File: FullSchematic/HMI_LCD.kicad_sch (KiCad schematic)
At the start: 31 parts, among them J10 LCD_Conn, J9 2x6 Pin Header, Q3 NPN, U10 SN74LVC2T45DCURE4, U11 SN74LVC2T45DCURE4, U12 SN74LVC2T45DCURE4, U13 SN74LVC2T45DCURE4, U14 SN74LV595ARGYR, U9 L79L05ABD13TR

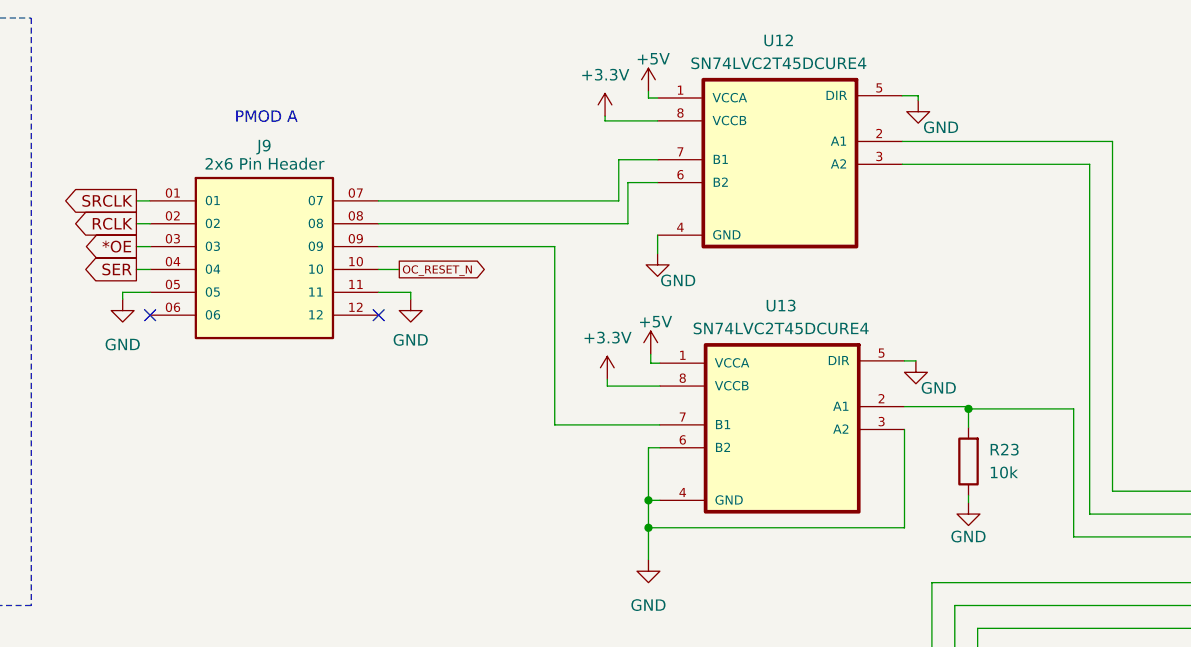
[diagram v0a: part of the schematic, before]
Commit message: Schematic/Footprint Update
Corrected Footprint / Schematic for PCB Design and Changed 10k Resistors to 0603 size.
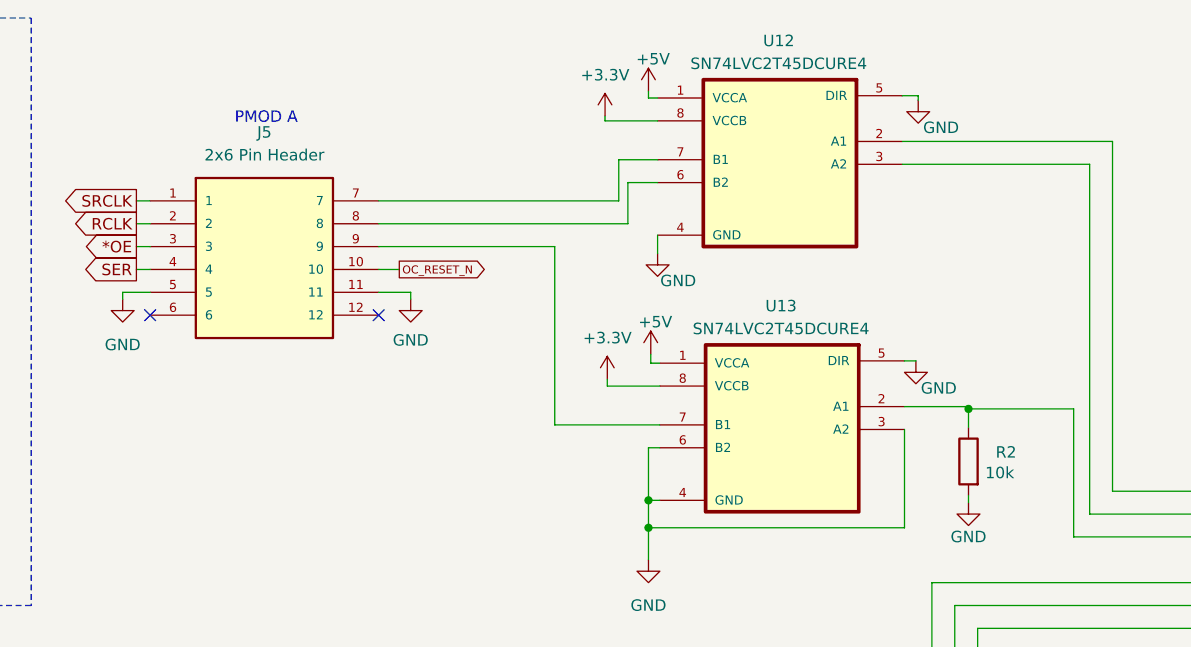
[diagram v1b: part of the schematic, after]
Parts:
- removed J9: 2x6 Pin Header, Connector_PinHeader_2.54mm:PinHeader_2x06_P2.54mm_Vertical, symbol SFMC-106-L2-L-D:SFMC-106-L2-L-D
- removed R23: 10k, Resistor_SMD:R_1206_3216Metric, symbol Device:R
- added J5: 2x6 Pin Header, Connector_PinHeader_2.54mm:PinHeader_2x06_P2.54mm_Vertical, symbol SFMC-106-L2-L-D:SFMC-106-L2-L-D
- added R2: 10k, Resistor_SMD:R_0201_0603Metric, symbol Device:R
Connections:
- net *OE: now also J5.3
- net GND: now also J5.11, J5.5, R2.2
- net OC_RESET_N: now also J5.10
- net RCLK: now also J5.2
- net SER: now also J5.4
- net SRCLK: now also J5.1
- net at J10.6 (E), U13.2 (A1): now also R2.1
- net at U13.7 (B1): now also J5.9
- net at U12.6 (B2): now also J5.8
- net at U12.7 (B1): now also J5.7

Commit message: Semi-complete board
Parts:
- J5: footprint Connector_PinHeader_2.54mm:PinHeader_2x06_P2.54mm_Vertical -> CustomFootprints:PMOD
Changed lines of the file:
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@@
       (effects (font (size 1.27 1.27)))
     )
-    (property "Footprint" "Connector_PinHeader_2.54mm:PinHeader_2x06_P2.54mm_Vertical" (at 118.0592 51.816 0)
+    (property "Footprint" "CustomFootprints:PMOD" (at 118.0592 51.816 0)
       (effects (font (size 1.27 1.27)) (justify bottom) hide)
     )

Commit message: PCB V.1
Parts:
- removed C3 (x4): .01u, Capacitor_SMD:C_0805_2012Metric, symbol Device:C
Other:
- moved on the sheet: C3

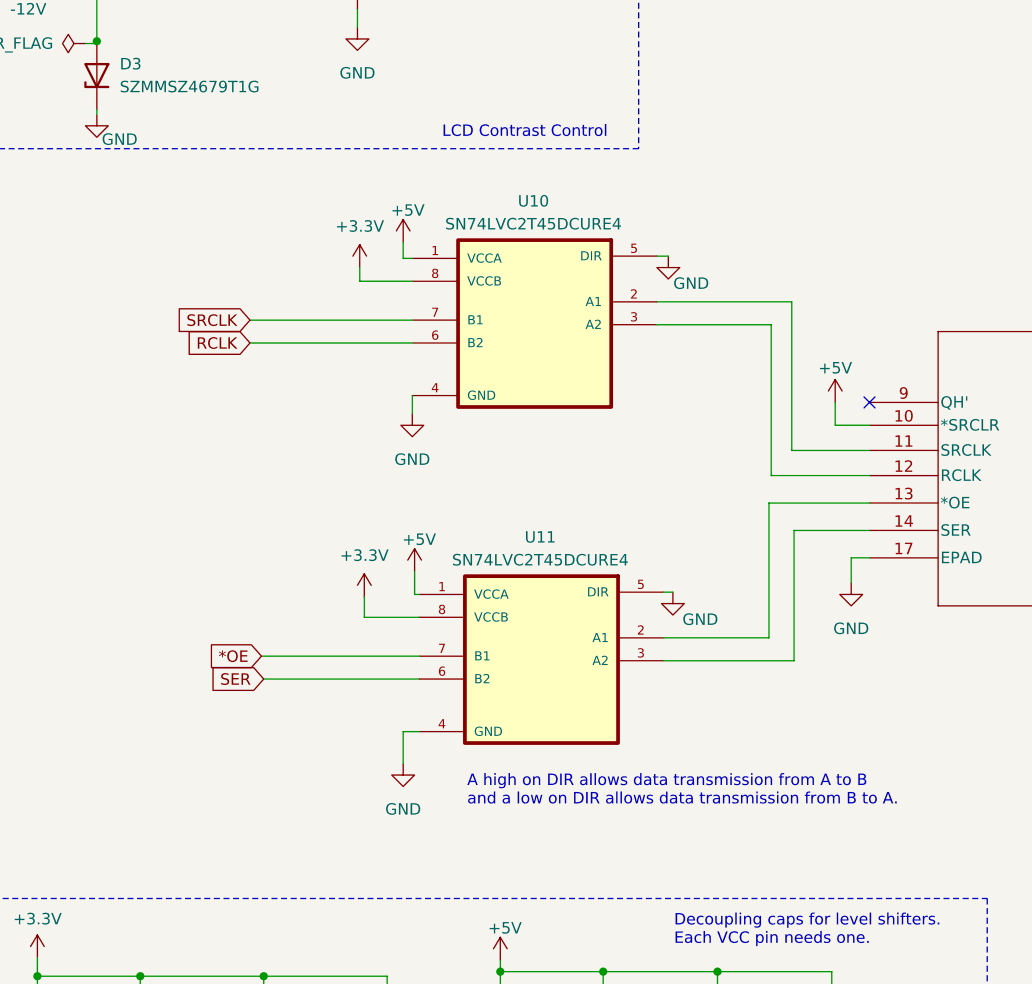
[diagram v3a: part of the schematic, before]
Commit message: Better LCD layout
Moved LCD to the top of the board, reorganized power planes to be better, more concise locations.
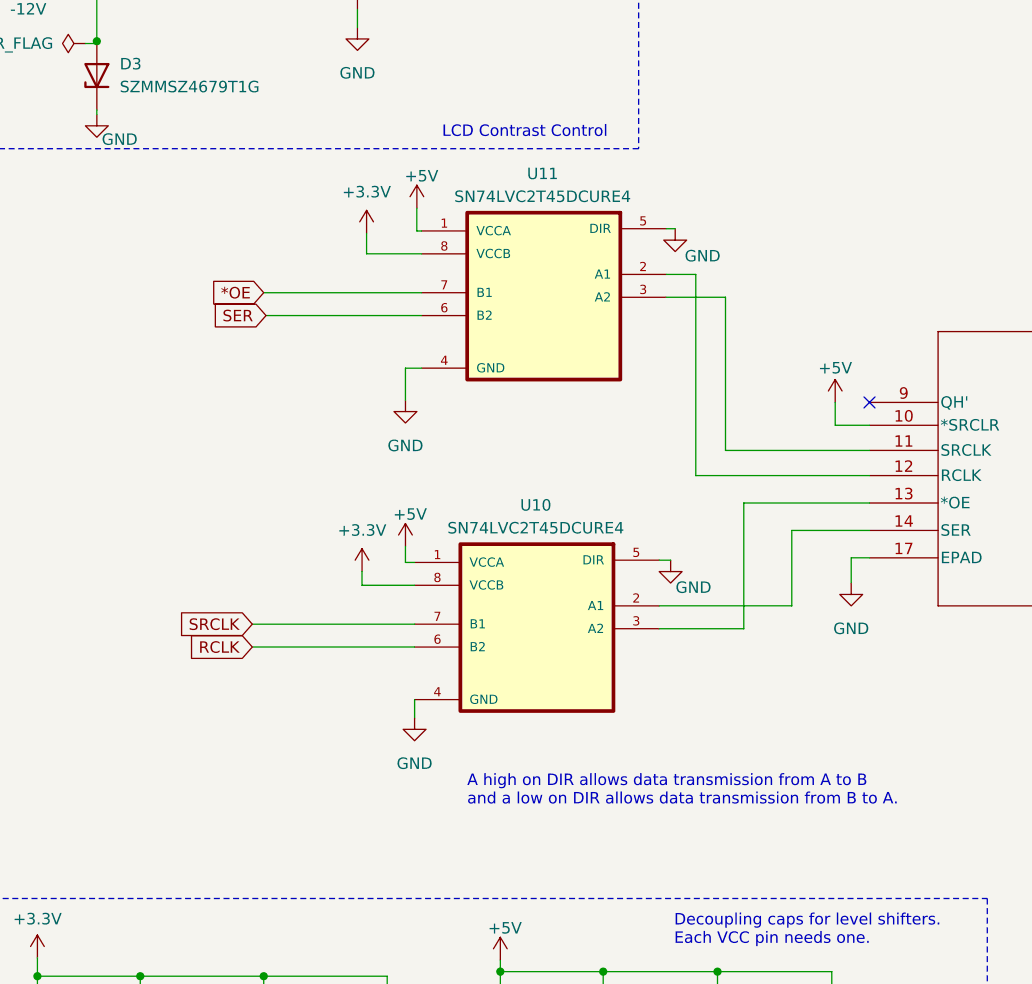
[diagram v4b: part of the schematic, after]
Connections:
- net at U11.2 (A1): now also U14.12 (RCLK); no longer U14.13 (*OE)
- net at U11.3 (A2): now also U14.11 (SRCLK); no longer U14.14 (SER)
- net at U10.2 (A1): now also U14.14 (SER); no longer U14.11 (SRCLK)
- net at U10.3 (A2): now also U14.13 (*OE); no longer U14.12 (RCLK)
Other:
- moved on the sheet: U10, U11

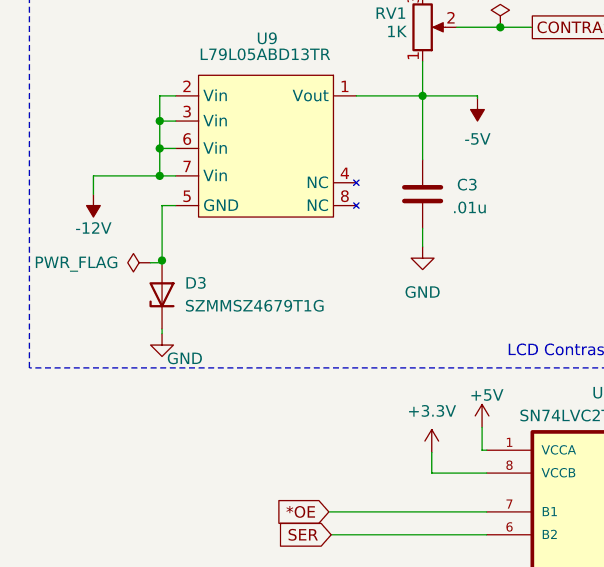
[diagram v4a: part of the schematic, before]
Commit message: Added silkscreen diodes for real
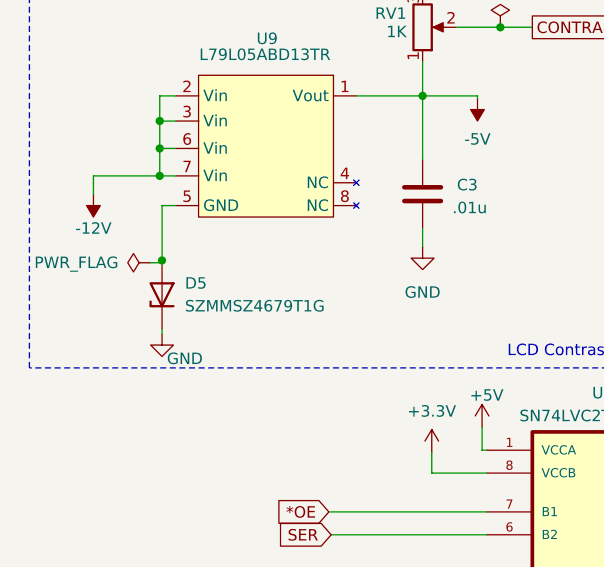
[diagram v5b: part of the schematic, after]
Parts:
- renumbered D3 to D5
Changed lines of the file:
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@@
   (symbol (lib_id "power:GND") (at 65.532 106.934 0) (mirror y) (unit 1)
     (in_bom yes) (on_board yes) (dnp no)
-    (property "Reference" "#PWR057" (at 65.532 113.284 0)
+    (property "Reference" "#PWR056" (at 65.532 113.284 0)
       (effects (font (size 1.27 1.27)) hide)
     )
@@
       (project "FullSchematic"
         (path "/650f0e66-3493-4c97-9577-99f99fcd23df/e50c3662-2ba3-4758-a6bd-15efafbf9fc3"
-          (reference "#PWR057") (unit 1)
+          (reference "#PWR056") (unit 1)
         )
       )
@@
   (symbol (lib_id "power:+5V") (at 65.532 123.19 0) (mirror y) (unit 1)
     (in_bom yes) (on_board yes) (dnp no)
-    (property "Reference" "#PWR056" (at 65.532 127 0)
+    (property "Reference" "#PWR057" (at 65.532 127 0)
       (effects (font (size 1.27 1.27)) hide)
     )
@@
       (project "FullSchematic"
         (path "/650f0e66-3493-4c97-9577-99f99fcd23df/e50c3662-2ba3-4758-a6bd-15efafbf9fc3"
-          (reference "#PWR056") (unit 1)
+          (reference "#PWR057") (unit 1)
         )
       )
@@
   (symbol (lib_id "Device:D_Zener") (at 31.242 70.866 90) (unit 1)
     (in_bom yes) (on_board yes) (dnp no) (fields_autoplaced)
-    (property "Reference" "D3" (at 33.782 69.596 90)
+    (property "Reference" "D5" (at 33.782 69.596 90)
       (effects (font (size 1.27 1.27)) (justify right))
     )
@@
       (project "FullSchematic"
         (path "/650f0e66-3493-4c97-9577-99f99fcd23df/e50c3662-2ba3-4758-a6bd-15efafbf9fc3"
-          (reference "D3") (unit 1)
-        )
-      )
+          (reference "D5") (unit 1)
+        )
+      )
